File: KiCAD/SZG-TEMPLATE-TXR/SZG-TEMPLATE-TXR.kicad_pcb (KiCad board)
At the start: 4 copper layers, 45 x 70 mm, 30 parts, among them J1 SYZYGY_TXR-4, J2 Conn_01x06, U1 ATtiny44A-MU

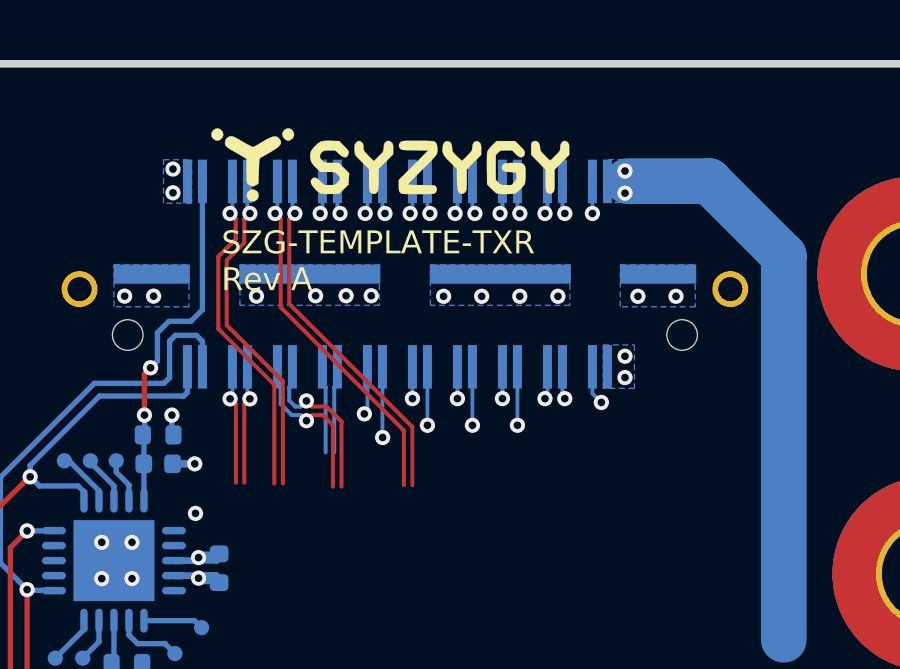
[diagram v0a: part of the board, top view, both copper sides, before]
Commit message: Corrected a net name. Improved example SYZYGY connector breakout routing for TXR board.
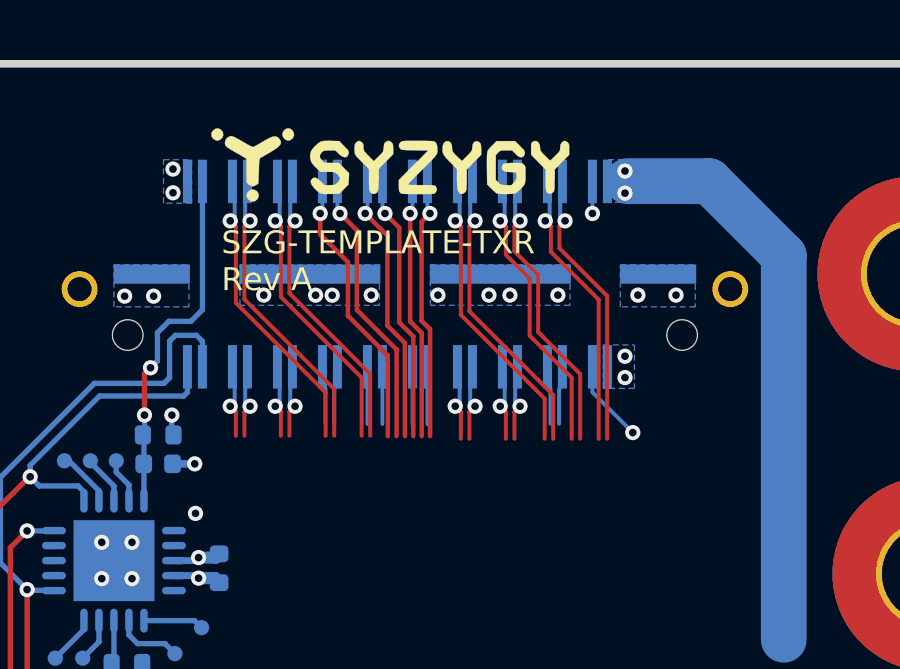
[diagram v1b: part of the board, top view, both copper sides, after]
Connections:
- net /RS3P renamed /RX3P
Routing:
- net /RX1P: track 5.52 -> 1.91 mm
- net /RX1N: track 5.52 -> 1.92 mm
- net /TX1P: track 11.9 -> 9.21 mm
- net /TX1N: track 11.9 -> 9.22 mm
- net /S2: track 4.48 -> 1.91 mm, vias 1 -> 0
- net /P2C_CLKN: track 4.01 -> 1.89 mm, vias 1 -> 0
- net /S6: track 4.01 -> 1.91 mm, vias 1 -> 0
- net /RX0P: track 3.98 -> 1.91 mm
- net /P2C_CLKP: track 4.01 -> 1.95 mm, vias 1 -> 0
- net /RX0N: track 3.98 -> 1.92 mm
- net /RX2P: track 4.01 -> 2.01 mm
- net /S4: track 3.90 -> 1.91 mm, vias 1 -> 0
- net /S8: track 3.90 -> 1.91 mm, vias 1 -> 0
- net /RX2N: track 4.01 -> 2.02 mm
- net /RX3P: track 4.00 -> 2.01 mm
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
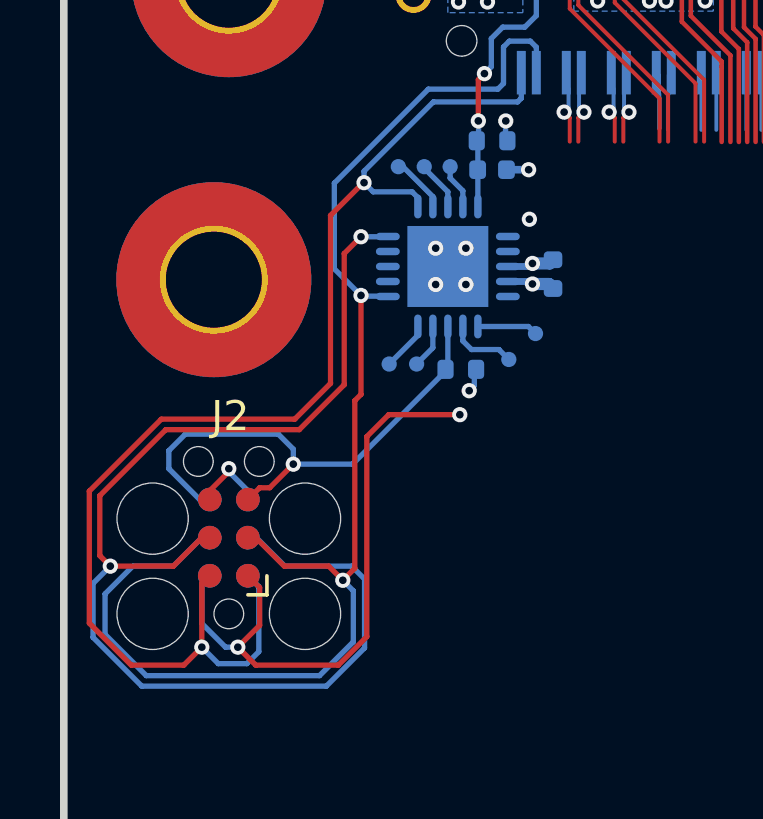
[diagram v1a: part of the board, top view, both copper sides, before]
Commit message: Updated the template projects MCU programming header to use the standard Tag-Connect cable pin order.
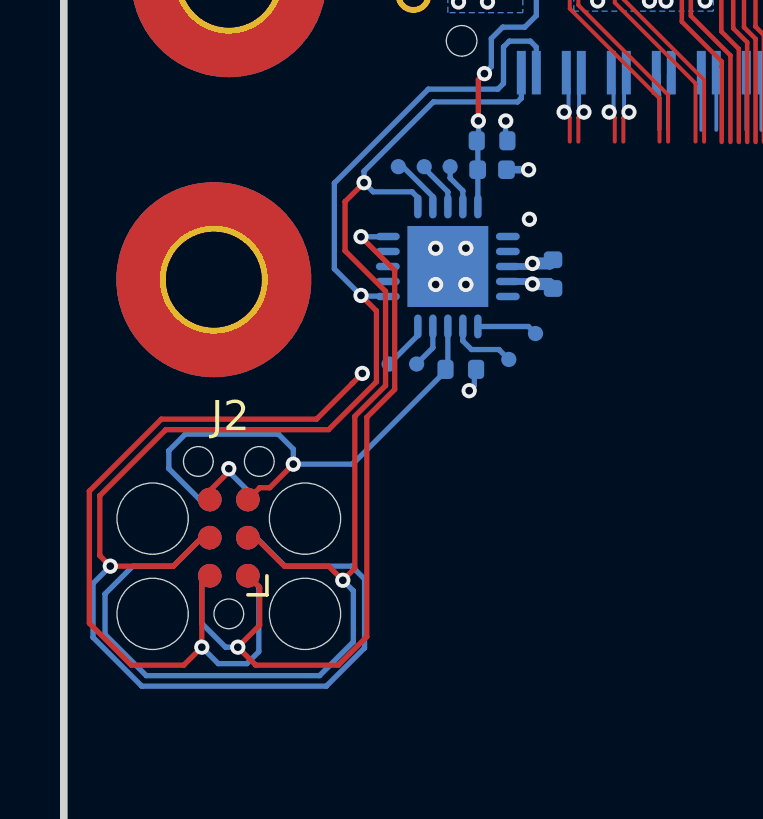
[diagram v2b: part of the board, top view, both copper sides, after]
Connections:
- J2 pad 1: +3V3 -> /MCU_MISO
- J2 pad 2: /MCU_SCL_USCK -> +3V3
- J2 pad 3: /MCU_SDA_MOSI -> /MCU_SCL_USCK
- J2 pad 4: /MCU_MISO -> /MCU_SDA_MOSI
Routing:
- net /MCU_MISO: track 41.6 -> 26.1 mm
- net /MCU_SDA_MOSI: track 46.2 -> 55.2 mm
- net +3V3: track 63.6 -> 69.7 mm
- net /MCU_SCL_USCK: track 42.7 -> 45.3 mm
- net +5V: track 26.7 -> 26.0 mm

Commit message: Fixed SZG-TEMPLATE-TXR board and mounting hole dimensions. Added TXR4 logo. Updated board images.
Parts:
- added REF**: SYZYGY_STD_Logo, SYZYGY:SYZYGY_TXR4_Logo, F.Cu at (126.6, 62.0)
- moved FID4 10.0 mm to (119.8, 70.6)
- moved FID5 10.0 mm to (119.8, 70.6)
- moved FID2 6.23 mm to (127.4, 126.0)
- moved FID7 6.23 mm to (127.4, 126.0)
- moved FID1 5.93 mm to (157.4, 126.0)
- moved FID8 5.93 mm to (157.4, 126.0)
- moved H3 2.50 mm to (122.4, 75.8)
- moved H4 2.50 mm to (162.4, 75.8)
- moved H5 2.50 mm to (122.4, 123.8)
- moved H6 2.50 mm to (162.4, 123.8)
- moved FID3 2.05 mm to (164.9, 61.4)
- moved FID6 2.05 mm to (164.9, 61.4)
- moved H1 1.91 mm to (123.5, 65.8)
- moved H2 1.91 mm to (161.3, 65.8)
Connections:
- H1 pad 1: Net-(H1-Pad1) -> unconnected-(H1-Pad1)
- H2 pad 1: Net-(H2-Pad1) -> unconnected-(H2-Pad1)
- H3 pad 1: Net-(H3-Pad1) -> unconnected-(H3-Pad1)
- H4 pad 1: Net-(H4-Pad1) -> unconnected-(H4-Pad1)
- H5 pad 1: Net-(H5-Pad1) -> unconnected-(H5-Pad1)
- H6 pad 1: Net-(H6-Pad1) -> unconnected-(H6-Pad1)
- U1 pad 10: Net-(U1-Pad10) -> unconnected-(U1-Pad10)
- U1 pad 17: Net-(U1-Pad17) -> unconnected-(U1-Pad17)
- U1 pad 18: Net-(U1-Pad18) -> unconnected-(U1-Pad18)
- U1 pad 19: Net-(U1-Pad19) -> unconnected-(U1-Pad19)
- U1 pad 6: Net-(U1-Pad6) -> unconnected-(U1-Pad6)
- U1 pad 7: Net-(U1-Pad7) -> unconnected-(U1-Pad7)
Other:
- board size 45 x 70 mm -> 50 x 70 mm
- net class Default removed
